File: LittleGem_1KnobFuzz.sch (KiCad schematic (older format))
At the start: 18 parts

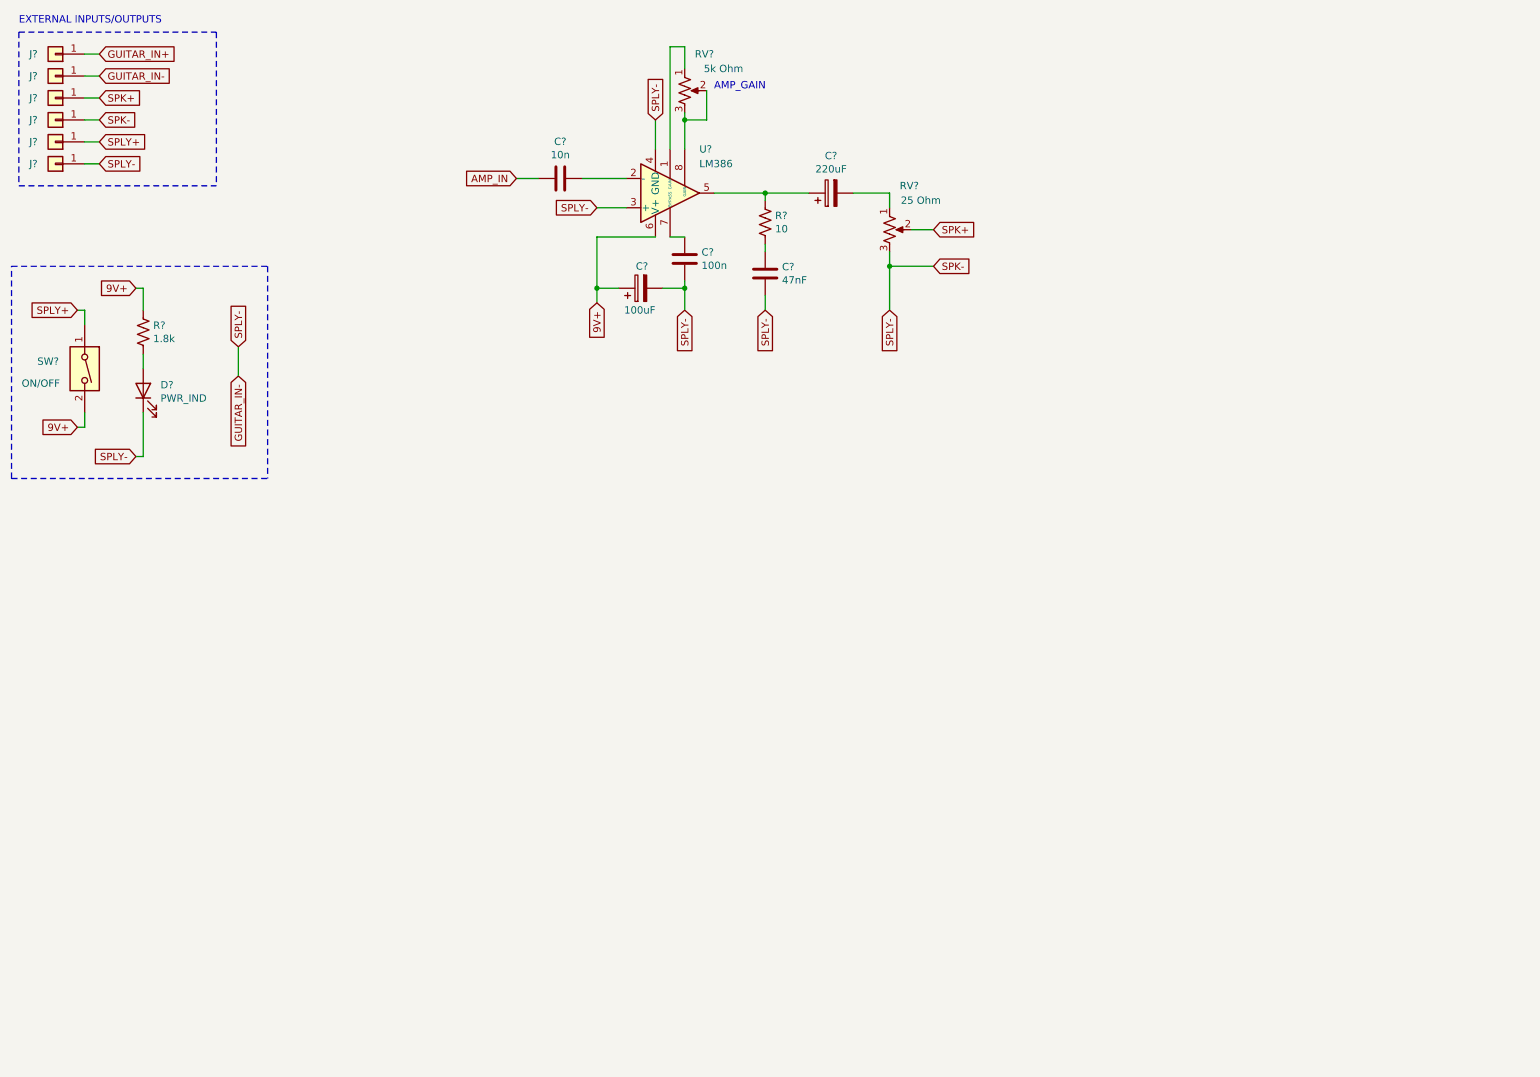
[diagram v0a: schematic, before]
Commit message: Add files via upload
finished the fuzz circuit, ready to breadboard and refine values now. Once values are refined, parts will be measured and PCB layout will begin
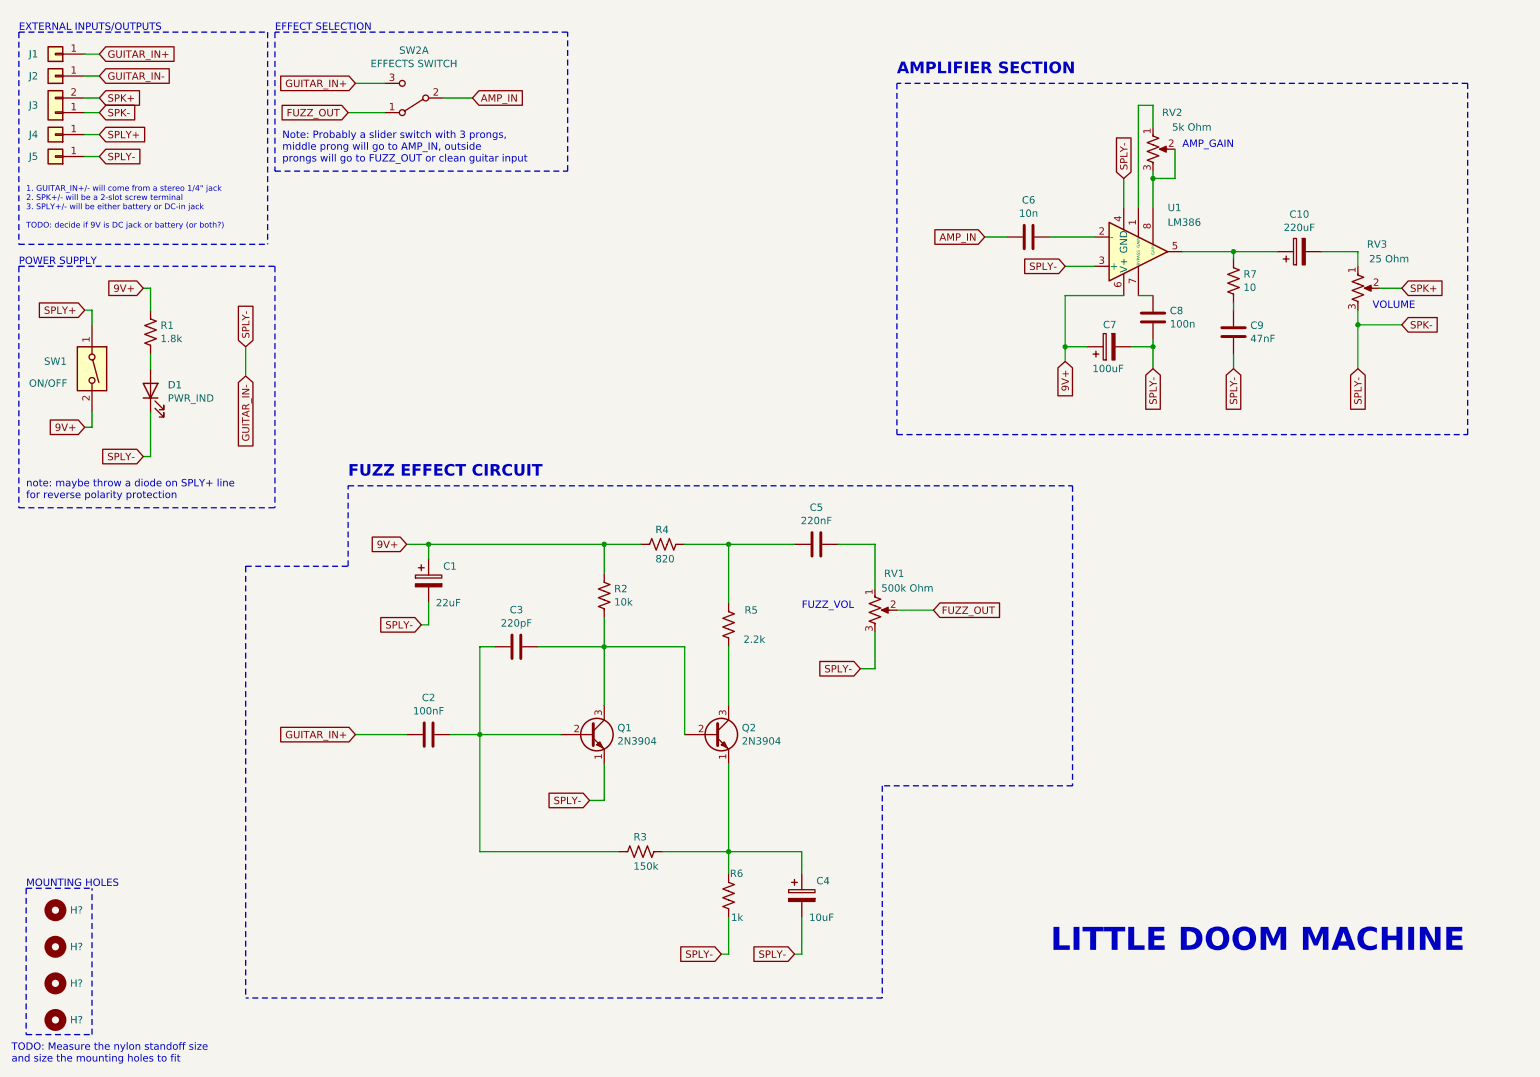
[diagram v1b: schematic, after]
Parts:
- removed J? (x2): Conn_01x01, symbol Connector_Generic:Conn_01x01
- added C1: 22uF, symbol Device:CP
- added C2: 100nF, symbol Device:C
- added C3: 220pF, symbol Device:C
- added C4: 10uF, symbol Device:CP
- added C5: 220nF, symbol Device:C
- added H? (x4): MountingHole, symbol Mechanical:MountingHole
- added J3: Conn_01x02, symbol Connector_Generic:Conn_01x02
- added Q1, Q2: 2N3904, Package_TO_SOT_THT:TO-92_Inline, symbol Transistor_BJT:2N3904
- added R2: 10k, symbol Device:R_US
- added R3: 150k, symbol Device:R_US
- added R4: 820, symbol Device:R_US
- added R5: 2.2k, symbol Device:R_US
- added R6: 1k, symbol Device:R_US
- added RV1: 500k Ohm, symbol Device:R_POT_US
- added SW2: EFFECTS SWITCH, symbol Switch:SW_DPDT_x2
- gave numbers to parts that had none: 16
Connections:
- net 9V+: now also C1.1, R2.1, R4.2
- net AMP_IN: now also SW2.2 (B)
- net GUITAR_IN+: now also C2.2, SW2.3 (C)
- net GUITAR_IN-: now also C1.2, C4.2, J3.1 (Pin_1), Q1.1 (E), R6.1, RV1.3
- net SPK+: now also J3.2 (Pin_2)
- new net: C2.1, C3.1, Q1.2 (B), R3.2
- new net: C3.2, Q1.3 (C), Q2.2 (B), R2.2
- new net: C4.1, Q2.1 (E), R3.1, R6.2
- new net: Q2.3 (C), R5.1
- new net: C5.1, R4.1, R5.2
- new net: C5.2, RV1.1
- new net FUZZ_OUT: RV1.2, SW2.1 (A)
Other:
- note added: "1. GUITAR_IN+/- will come from a stereo 1/4" jack\n2. SPK+/- will be a 2-slot screw terminal\n3. SPLY+/- will be either battery or DC-in jack\n\nTODO: decide if 9V is DC jack or battery (or both?)"
- note added: "AMPLIFIER SECTION"
- note added: "EFFECT SELECTION"
- note added: "FUZZ EFFECT CIRCUIT"
- note added: "FUZZ_VOL"
- note added: "LITTLE DOOM MACHINE"
- note added: "MOUNTING HOLES"
- note added: "Note: Probably a slider switch with 3 prongs, \nmiddle prong will go to AMP_IN, outside \nprongs will go to FUZZ_OUT or clean guitar input"
- note added: "POWER SUPPLY"
- note added: "TODO: Measure the nylon standoff size\nand size the mounting holes to fit"
- note added: "VOLUME"
- note added: "note: maybe throw a diode on SPLY+ line \nfor reverse polarity protection"
- moved on the sheet: C10, C6, C7, C8, C9, D1, J4, J5, R1, R7, RV2, RV3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
